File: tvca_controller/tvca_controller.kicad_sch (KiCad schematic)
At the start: 12 parts, among them J1 Conn_01x05_Socket, U1 MCP2562, U2 PIC18F26K83, Y1 Crystal

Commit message: tiny ass random change to ensure I can do git stuff
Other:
- title: T.V.C.A Controller -> T.V.C.A. Controller
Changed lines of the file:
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@@
   (paper "A4")
   (title_block
-    (title "T.V.C.A Controller")
+    (title "T.V.C.A. Controller")
     (date "2024-05-11")
     (rev "0.0.1")

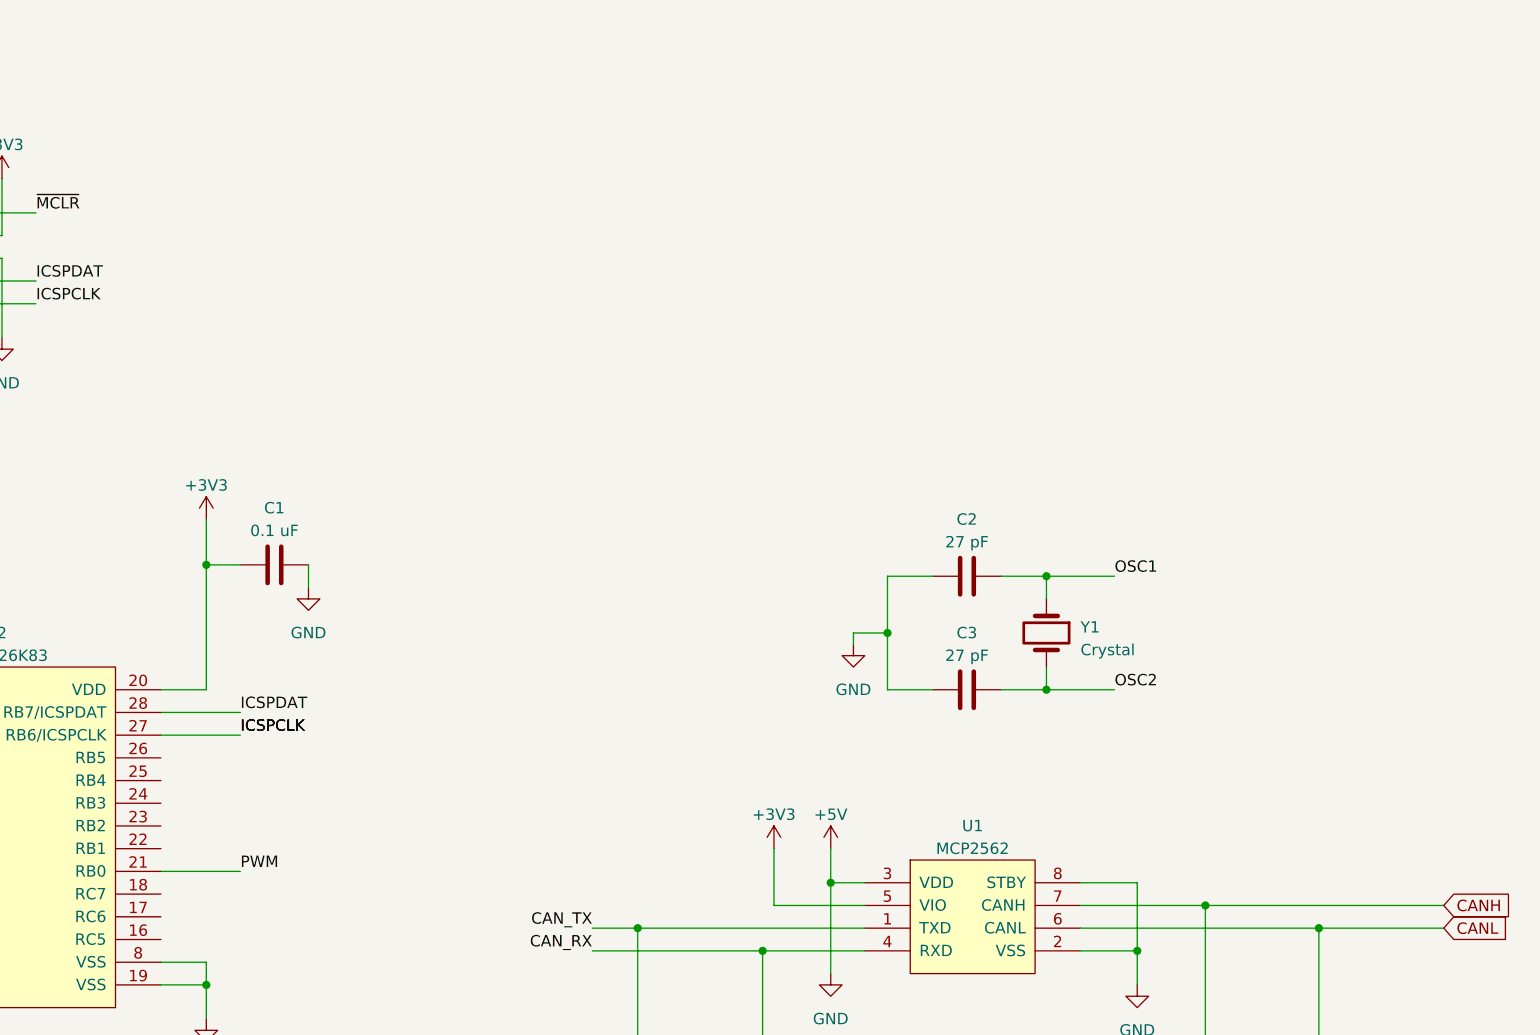
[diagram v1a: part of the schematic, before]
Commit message: get basic motor control logic going
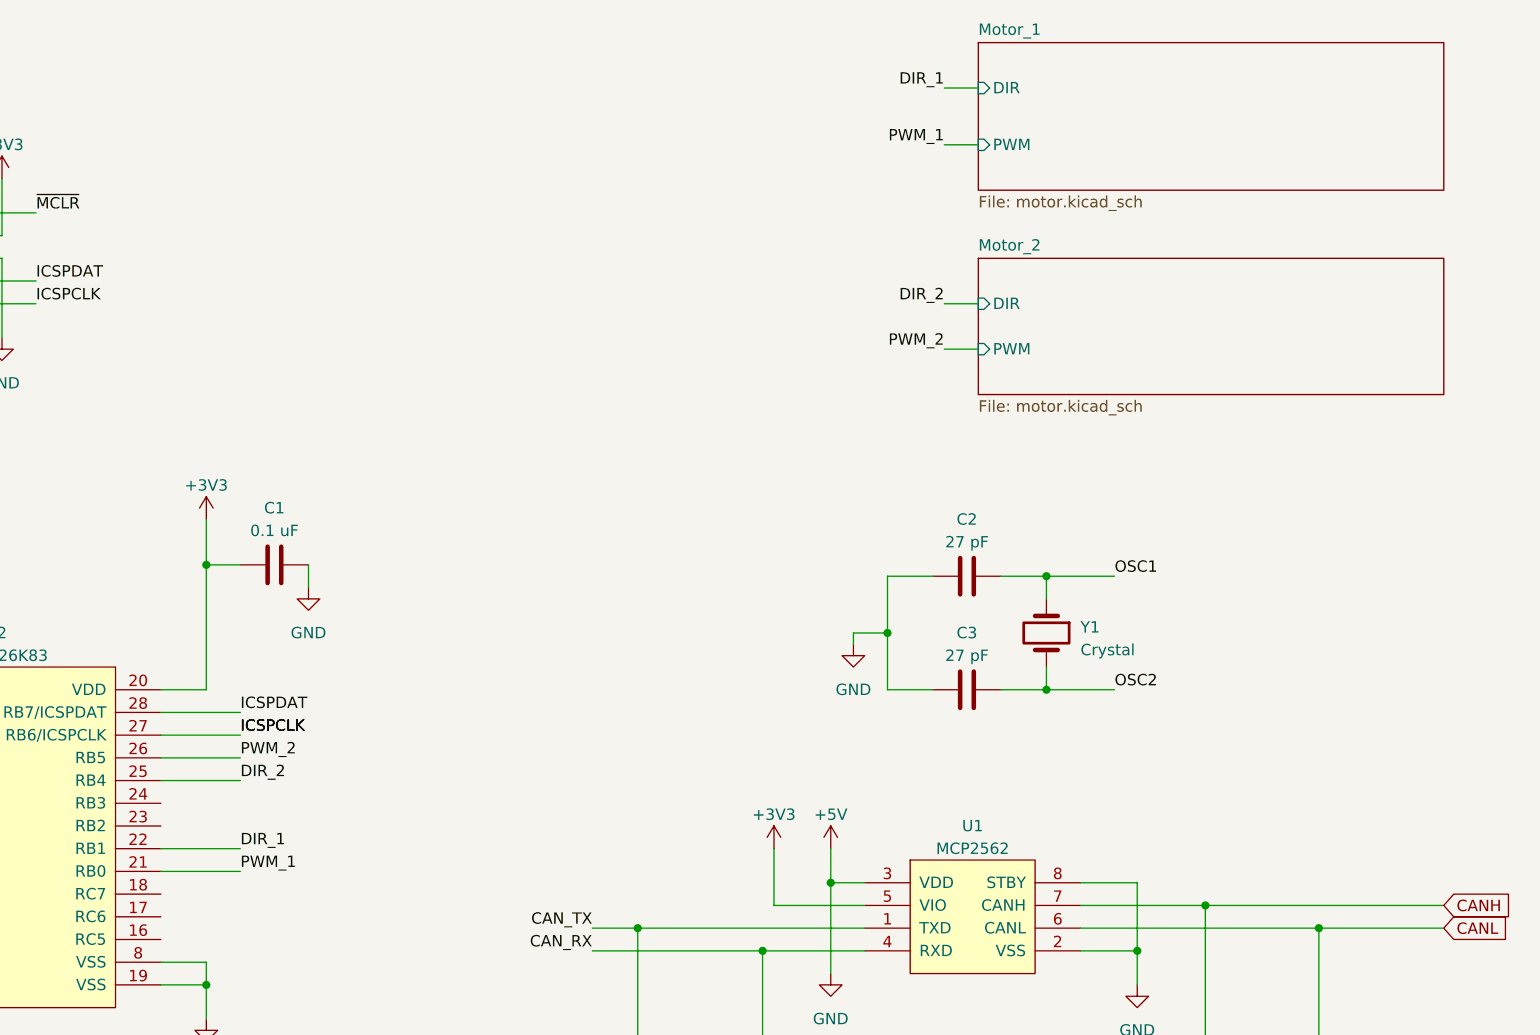
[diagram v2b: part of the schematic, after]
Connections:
- net DIR_1: now reaches U2.22 (RB1)
- net DIR_2: now reaches U2.25 (RB4)
- net PWM_2: now reaches U2.26 (RB5)
- net PWM renamed PWM_1
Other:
- added sheet Motor_1 (motor.kicad_sch)
- added sheet Motor_2 (motor.kicad_sch)
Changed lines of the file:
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@@
+    (stroke (width 0) (type default))
+  )
+  (wire (pts (xy 171.45 53.34) (xy 175.26 53.34))
     (stroke (width 0) (type default))
   )
@@
     (stroke (width 0) (type default))
   )
+  (wire (pts (xy 83.82 124.46) (xy 92.71 124.46))
+    (stroke (width 0) (type default))
+  )
   (wire (pts (xy 88.9 100.33) (xy 92.71 100.33))
     (stroke (width 0) (type default))
   )
+  (wire (pts (xy 171.45 76.2) (xy 175.26 76.2))
+    (stroke (width 0) (type default))
+  )
   (wire (pts (xy 62.23 68.58) (xy 69.85 68.58))
     (stroke (width 0) (type default))
@@
     (stroke (width 0) (type default))
   )
+  (wire (pts (xy 83.82 121.92) (xy 92.71 121.92))
+    (stroke (width 0) (type default))
+  )
   (wire (pts (xy 151.13 143.51) (xy 162.56 143.51))
     (stroke (width 0) (type default))
@@
     (stroke (width 0) (type default))
   )
+  (wire (pts (xy 171.45 46.99) (xy 175.26 46.99))
+    (stroke (width 0) (type default))
+  )
   (wire (pts (xy 39.37 132.08) (xy 46.99 132.08))
     (stroke (width 0) (type default))
@@
     (stroke (width 0) (type default))
   )
+  (wire (pts (xy 171.45 71.12) (xy 175.26 71.12))
+    (stroke (width 0) (type default))
+  )
   (wire (pts (xy 158.75 135.89) (xy 158.75 146.05))
     (stroke (width 0) (type default))
@@
     (stroke (width 0) (type default))
   )
+  (wire (pts (xy 83.82 132.08) (xy 92.71 132.08))
+    (stroke (width 0) (type default))
+  )
   (wire (pts (xy 165.1 107.95) (xy 161.29 107.95))
     (stroke (width 0) (type default))
@@
     (stroke (width 0) (type default))
   )
+  (label "PWM_2" (at 92.71 121.92 0) (fields_autoplaced)
+    (effects (font (size 1.27 1.27)) (justify left bottom))
+  )
   (label "ICSPDAT" (at 69.85 68.58 0) (fields_autoplaced)
     (effects (font (size 1.27 1.27)) (justify left bottom))
@@
     (effects (font (size 1.27 1.27)) (justify left bottom))
   )
+  (label "DIR_2" (at 92.71 124.46 0) (fields_autoplaced)
+    (effects (font (size 1.27 1.27)) (justify left bottom))
+  )
   (label "CAN_TX" (at 132.08 140.97 180) (fields_autoplaced)
     (effects (font (size 1.27 1.27)) (justify right bottom))
@@
     (effects (font (size 1.27 1.27)) (justify right bottom))
   )
-  (label "PWM" (at 92.71 134.62 0) (fields_autoplaced)
+  (label "DIR_1" (at 92.71 132.08 0) (fields_autoplaced)
+    (effects (font (size 1.27 1.27)) (justify left bottom))
+  )
+  (label "PWM_1" (at 171.45 53.34 180) (fields_autoplaced)
+    (effects (font (size 1.27 1.27)) (justify right bottom))
+  )
+  (label "DIR_1" (at 171.45 46.99 180) (fields_autoplaced)
+    (effects (font (size 1.27 1.27)) (justify right bottom))
+  )
+  (label "PWM_1" (at 92.71 134.62 0) (fields_autoplaced)
     (effects (font (size 1.27 1.27)) (justify left bottom))
   )
@@
     (effects (font (size 1.27 1.27)) (justify right bottom))
   )
+  (label "DIR_2" (at 171.45 71.12 180) (fields_autoplaced)
+    (effects (font (size 1.27 1.27)) (justify right bottom))
+  )
   (label "~{MCLR}" (at 69.85 60.96 0) (fields_autoplaced)
     (effects (font (size 1.27 1.27)) (justify left bottom))
+  )
+  (label "PWM_2" (at 171.45 76.2 180) (fields_autoplaced)
+    (effects (font (size 1.27 1.27)) (justify right bottom))
   )
   (label "ICSPCLK" (at 69.85 71.12 0) (fields_autoplaced)
@@
       )
     )
+  )
+  (sheet (at 175.26 66.04) (size 52.07 15.24) (fields_autoplaced)
+    (stroke (width 0.1524) (type solid))
+    (fill (color 0 0 0 0.0000))
+    (property "Sheetname" "Motor_2" (at 175.26 65.3284 0)
+      (effects (font (size 1.27 1.27)) (justify left bottom))
+    )
+    (property "Sheetfile" "motor.kicad_sch" (at 175.26 81.8646 0)
+      (effects (font (size 1.27 1.27)) (justify left top))
+    )
+    (property "Field2" "" (at 175.26 66.04 0)
+      (effects (font (size 1.27 1.27)) hide)
+    )
+    (pin "PWM" input (at 175.26 76.2 180)
+      (effects (font (size 1.27 1.27)) (justify left))
+    )
+    (pin "DIR" input (at 175.26 71.12 180)
+      (effects (font (size 1.27 1.27)) (justify left))
+    )
+    (instances
+      (project "tvca_controller"
+        (path "/f08602f6-65d5-48ec-b5dd-079a575e1be0" (page "3"))
+      )
+    )
+  )
+  (sheet (at 175.26 41.91) (size 52.07 16.51) (fields_autoplaced)
+    (stroke (width 0.1524) (type solid))
+    (fill (color 0 0 0 0.0000))
+    (property "Sheetname" "Motor_1" (at 175.26 41.1984 0)
+      (effects (font (size 1.27 1.27)) (justify left bottom))
+    )
+    (property "Sheetfile" "motor.kicad_sch" (at 175.26 59.0046 0)
+      (effects (font (size 1.27 1.27)) (justify left top))
+    )
+    (pin "DIR" input (at 175.26 46.99 180)
+      (effects (font (size 1.27 1.27)) (justify left))
+    )
+    (pin "PWM" input (at 175.26 53.34 180)
+      (effects (font (size 1.27 1.27)) (justify left))
+    )
+    (instances
+      (project "tvca_controller"
+        (path "/f08602f6-65d5-48ec-b5dd-079a575e1be0" (page "2"))
+      )
+    )

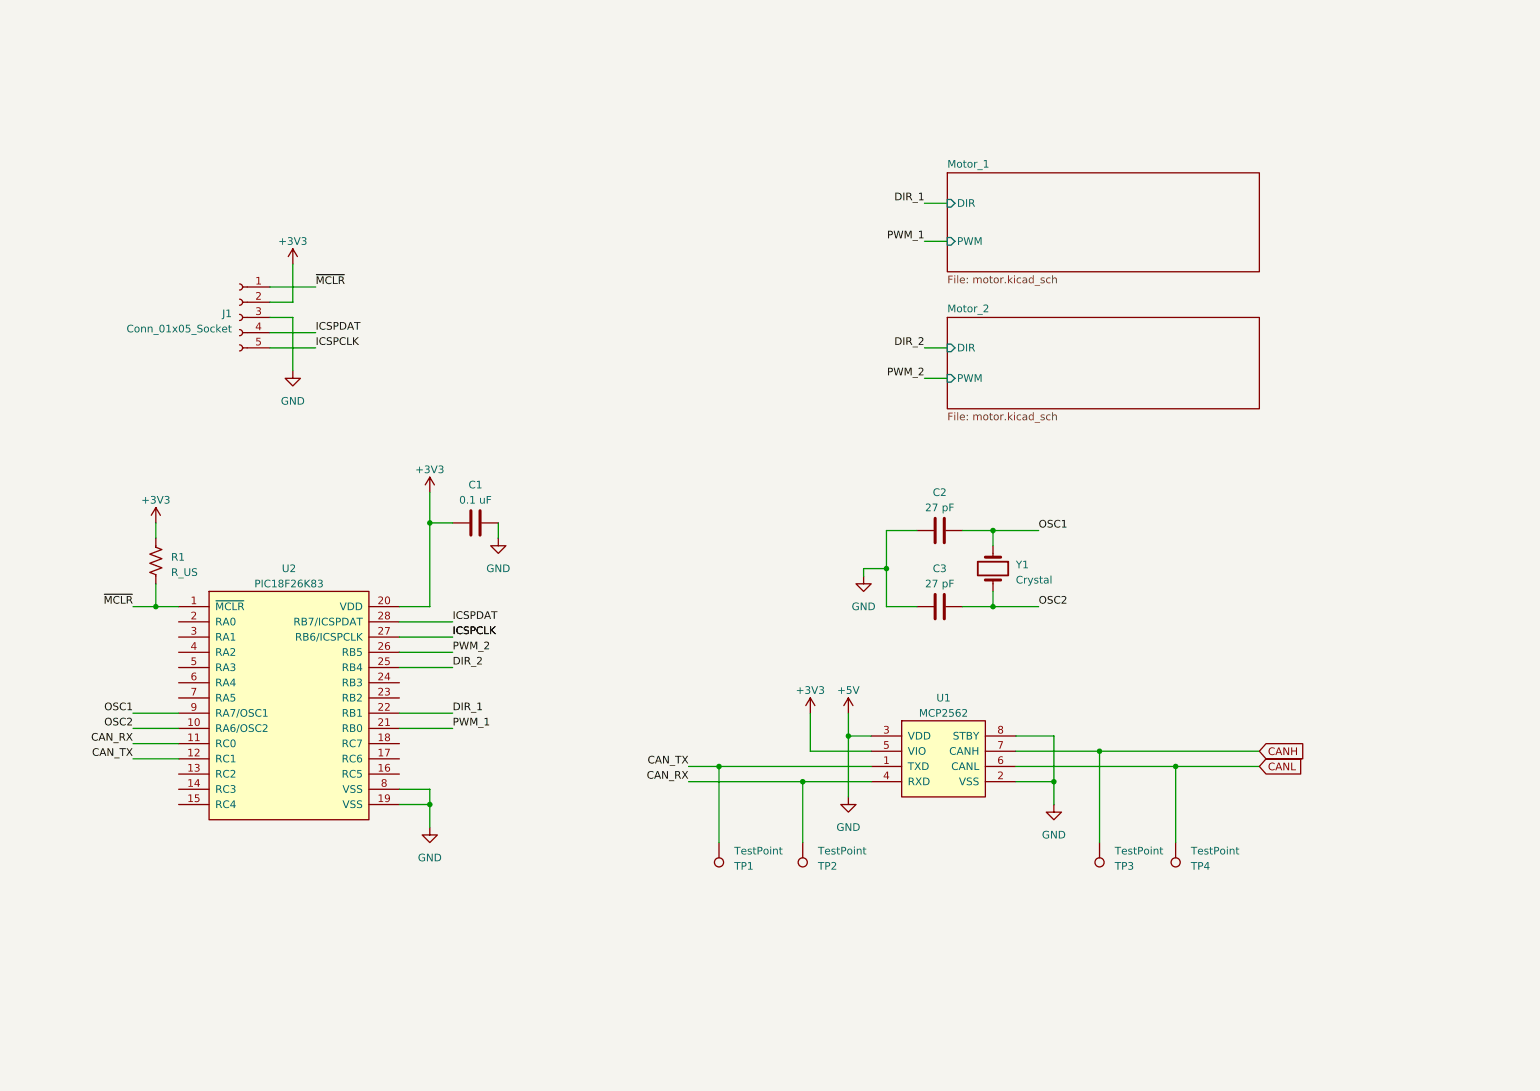
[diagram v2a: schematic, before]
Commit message: add can connector, and git ignore
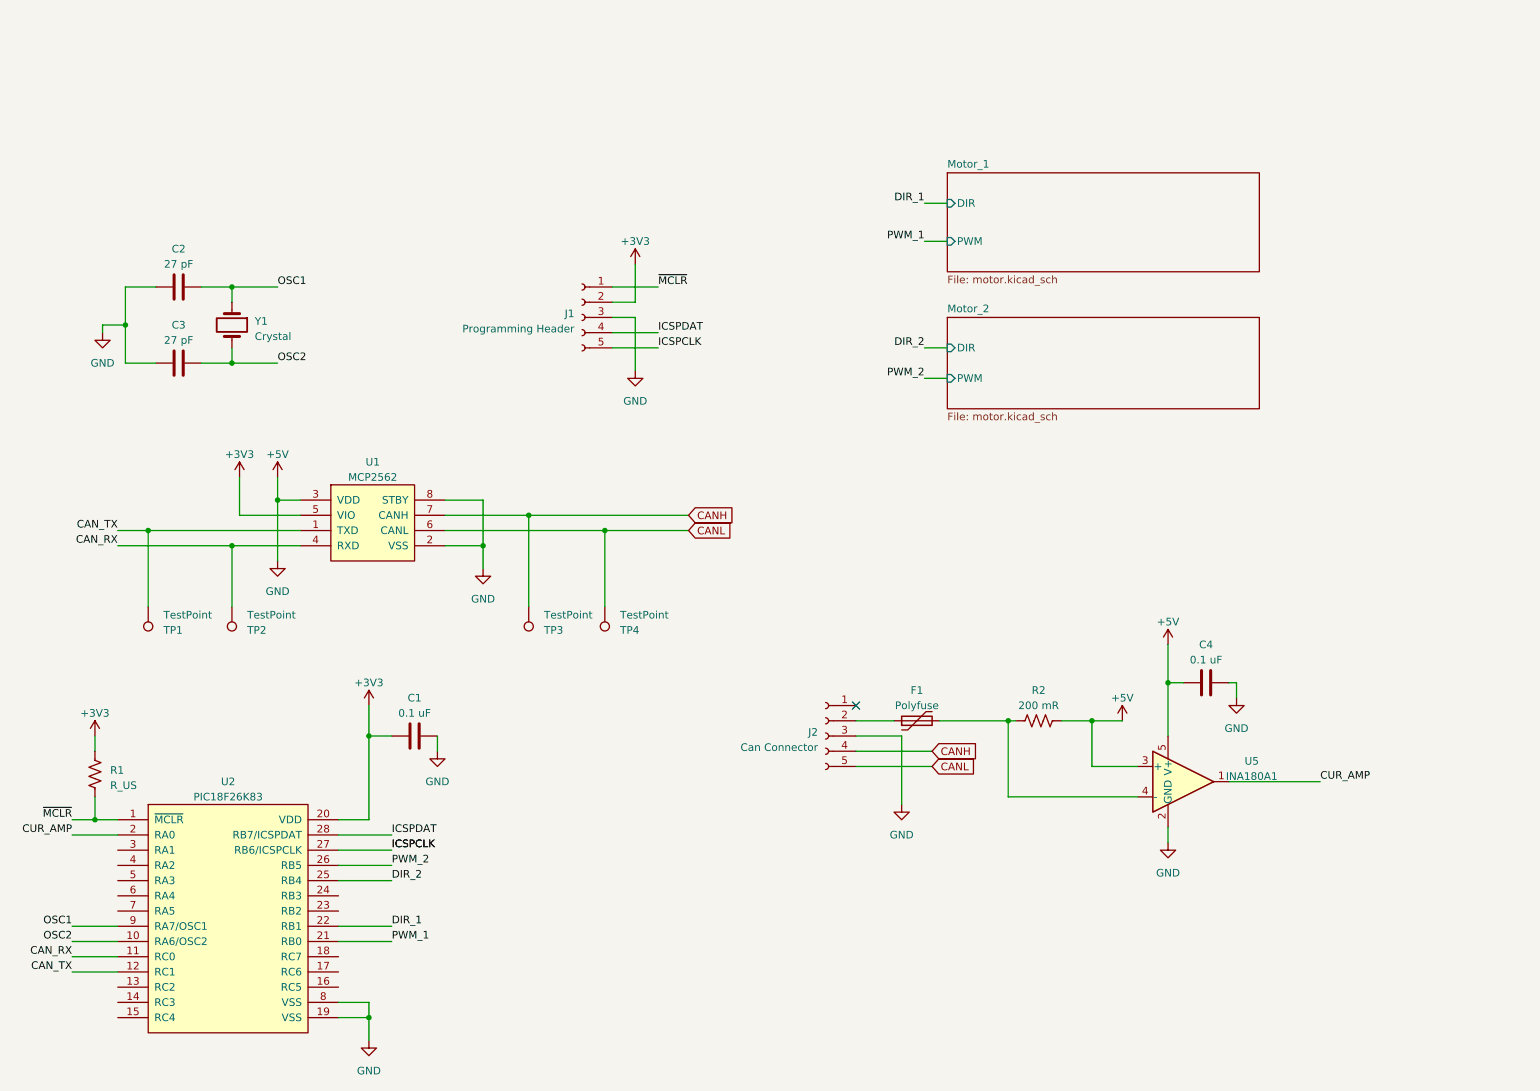
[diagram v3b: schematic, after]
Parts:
- added C4: 0.1 uF, symbol Device:C
- added F1: Polyfuse, symbol Device:Polyfuse
- added J2: Can Connector, symbol Connector:Conn_01x05_Socket
- added R2: 200 mR, symbol Device:R_US
- added U5: INA180A1, Package_TO_SOT_SMD:SOT-23-5, symbol Amplifier_Current:INA180A1
- J1: value Conn_01x05_Socket -> Programming Header
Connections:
- net +5V: now also C4.1, C4.2, J2.3 (Pin_3), R2.1, U5.2 (GND), U5.3 (+), U5.5 (V+)
- net CANH: now also J2.4 (Pin_4)
- net CANL: now also J2.5 (Pin_5)
- net CUR_AMP: now reaches U2.2 (RA0)
- net CUR_AMP: now also U5.1
- new net: F1.1, J2.2 (Pin_2)
- new net: F1.2, R2.2, U5.4 (-)
- no-connect marks 0 -> 1
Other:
- moved on the sheet: C1, C2, C3, J1, R1, TP1, TP2, TP3, TP4, U1, U2, Y1
